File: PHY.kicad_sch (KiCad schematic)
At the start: 19 parts, among them U11 LAN8742A, Y2 25Mhz

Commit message: change cad data
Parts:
- removed C39, C40: 15pF, Capacitor_SMD:C_0603_1608Metric_Pad1.08x0.95mm_HandSolder, symbol Device:C
- removed Y2: 25Mhz, Crystal:Crystal_SMD_SeikoEpson_FA238-4Pin_3.2x2.5mm, symbol Device:Crystal
- added C55, C56, C60: 100n, Capacitor_SMD:C_0603_1608Metric_Pad1.08x0.95mm_HandSolder, symbol Device:C_Small
- added C57, C58: 15pF, Capacitor_SMD:C_0603_1608Metric_Pad1.08x0.95mm_HandSolder, symbol Device:C
- added C62: 1u, Capacitor_SMD:C_0603_1608Metric_Pad1.08x0.95mm_HandSolder, symbol Device:C_Small
- added C63: 470p, Capacitor_SMD:C_0603_1608Metric_Pad1.08x0.95mm_HandSolder, symbol Device:C_Small
- added D10, D11: LED, LED_SMD:LED_0603_1608Metric_Pad1.05x0.95mm_HandSolder, symbol Device:LED
- added R51, R52: 1k, Resistor_SMD:R_0603_1608Metric_Pad0.98x0.95mm_HandSolder, symbol Device:R
- added Y3: 25Mhz, Crystal:Crystal_SMD_SeikoEpson_FA128-4Pin_2.0x1.6mm, symbol Device:Crystal_GND24
- renumbered FB1 to FB3, R24 to R31, R23 to R32, R22 to R33, R25 to R34, R26 to R35, R27 to R36, R28 to R37, R32 to R42, R29 to R43, R36 to R44, R33 to R45, R37 to R46, R39 to R47, R38 to R48, U11 to U12
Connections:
- net +3.3V: now also U12.9 (VDDIO), C56.1
- net GND: now also C55.2, C56.2, C57.2, C58.2, C60.2, C62.2, C63.2, D10.1 (K), D11.1 (K), Y3.2, Y3.4
- net at FB3.2, R35.1, R37.1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: now also C55.1, C60.1
- net at U12.2 (LED2/~{INTSEL}): now also R52.1
- net at U12.3 (LED1/REGOFF): now also R51.1
- net at U12.4 (XTAL2): now also C57.1, Y3.3
- net at U12.5 (XTAL1/CLKIN): now also C58.1, Y3.1
- net at U12.6 (VDDCR): now also C62.1, C63.1
- new net: D10.2 (A), R51.2
- new net: D11.2 (A), R52.2
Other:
- moved on the sheet: R35, R37, R42, R44

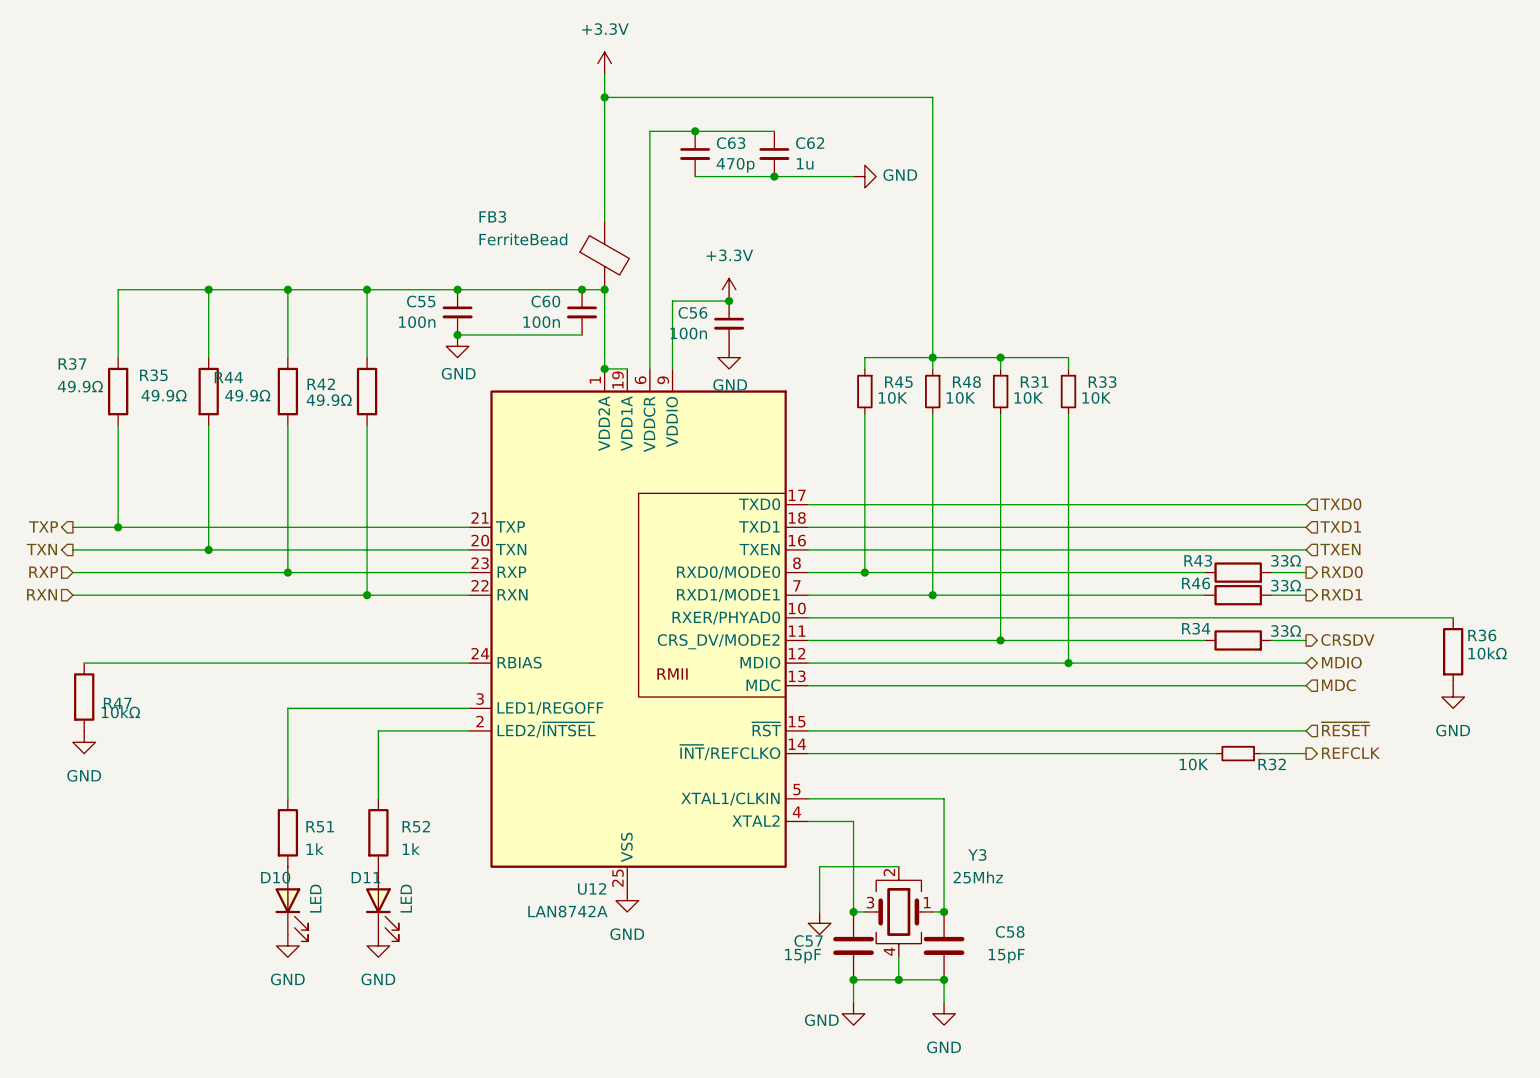
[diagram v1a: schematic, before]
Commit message: remove efuse
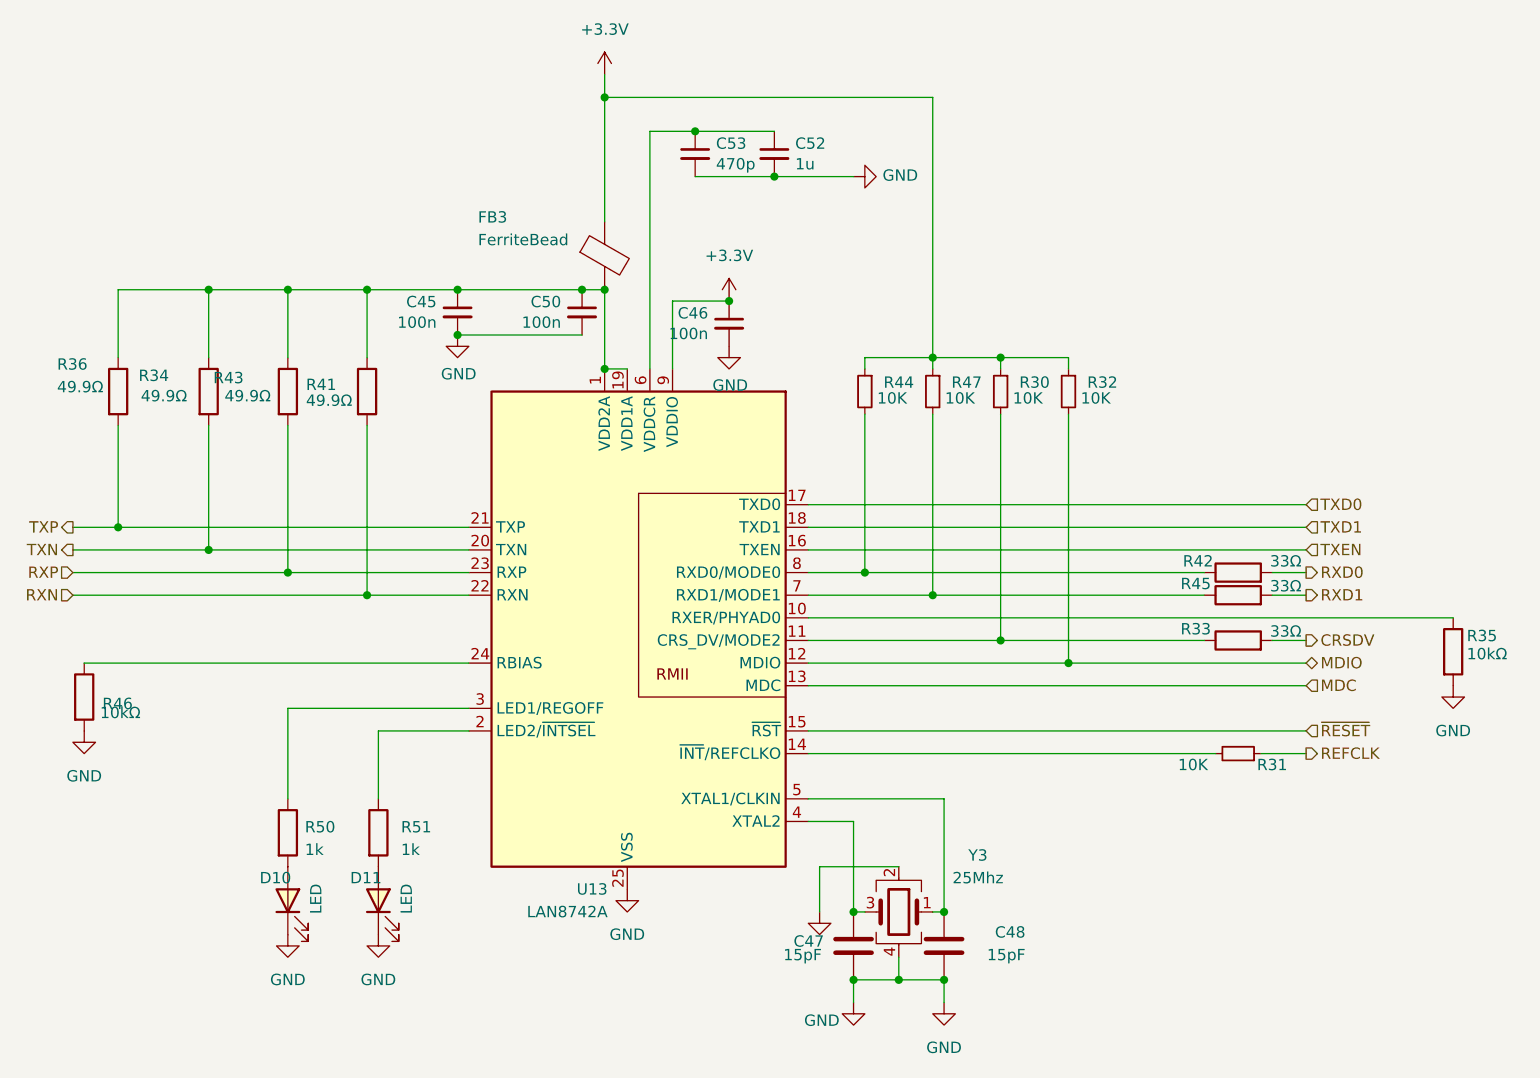
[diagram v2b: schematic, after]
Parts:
- renumbered C55 to C45, C56 to C46, C57 to C47, C58 to C48, C60 to C50, C62 to C52, C63 to C53, R31 to R30, R32 to R31, R33 to R32, R34 to R33, R35 to R34, R36 to R35, R37 to R36, R42 to R41, R43 to R42, R44 to R43, R45 to R44, R46 to R45, R47 to R46, R48 to R47, R51 to R50, R52 to R51, U12 to U13
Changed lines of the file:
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@@
 		(on_board yes)
 		(dnp no)
-		(property "Reference" "R46"
+		(property "Reference" "R45"
 			(at 206.502 115.57 90)
 			(effects
@@
 			(project "mainboard4"
 				(path "/dd07ab80-a59c-44f4-ac7d-849e21e1384e/4fc6aed4-b6ec-46a7-b9d1-1f9060000df7"
-					(reference "R46")
+					(reference "R45")
 					(unit 1)
 				)
@@
 		(on_board yes)
 		(dnp no)
-		(property "Reference" "R44"
+		(property "Reference" "R43"
 			(at 94.488 92.456 0)
 			(effects
@@
 			(project "mainboard4"
 				(path "/dd07ab80-a59c-44f4-ac7d-849e21e1384e/4fc6aed4-b6ec-46a7-b9d1-1f9060000df7"
-					(reference "R44")
+					(reference "R43")
 					(unit 1)
 				)
@@
 		(on_board yes)
 		(dnp no)
-		(property "Reference" "C56"
+		(property "Reference" "C46"
 			(at 150.0632 85.1916 0)
 			(effects
@@
 			(project "mainboard4"
 				(path "/dd07ab80-a59c-44f4-ac7d-849e21e1384e/4fc6aed4-b6ec-46a7-b9d1-1f9060000df7"
-					(reference "C56")
+					(reference "C46")
 					(unit 1)
 				)
@@
 		(on_board yes)
 		(dnp no)
-		(property "Reference" "C60"
+		(property "Reference" "C50"
 			(at 133.5532 83.9216 0)
 			(effects
@@
 			(project "mainboard4"
 				(path "/dd07ab80-a59c-44f4-ac7d-849e21e1384e/4fc6aed4-b6ec-46a7-b9d1-1f9060000df7"
-					(reference "C60")
+					(reference "C50")
 					(unit 1)
 				)
@@
 		(on_board yes)
 		(dnp no)
-		(property "Reference" "R47"
+		(property "Reference" "R46"
 			(at 82.042 129.032 0)
 			(effects
@@
 			(project "mainboard4"
 				(path "/dd07ab80-a59c-44f4-ac7d-849e21e1384e/4fc6aed4-b6ec-46a7-b9d1-1f9060000df7"
-					(reference "R47")
+					(reference "R46")
 					(unit 1)
 				)
@@
 		(on_board yes)
 		(dnp no)
-		(property "Reference" "R37"
+		(property "Reference" "R36"
 			(at 76.962 90.932 0)
 			(effects
@@
 			(project "mainboard4"
 				(path "/dd07ab80-a59c-44f4-ac7d-849e21e1384e/4fc6aed4-b6ec-46a7-b9d1-1f9060000df7"
-					(reference "R37")
+					(reference "R36")
 					(unit 1)
 				)
@@
 		(on_board yes)
 		(dnp no)
-		(property "Reference" "U12"
+		(property "Reference" "U13"
 			(at 138.7759 149.86 0)
 			(effects
@@
 			(project "mainboard4"
 				(path "/dd07ab80-a59c-44f4-ac7d-849e21e1384e/4fc6aed4-b6ec-46a7-b9d1-1f9060000df7"
-					(reference "U12")
+					(reference "U13")
 					(unit 1)
 				)
@@
 		(on_board yes)
 		(dnp no)
-		(property "Reference" "R43"
+		(property "Reference" "R42"
 			(at 206.756 113.03 90)
 			(effects
@@
 			(project "mainboard4"
 				(path "/dd07ab80-a59c-44f4-ac7d-849e21e1384e/4fc6aed4-b6ec-46a7-b9d1-1f9060000df7"
-					(reference "R43")
+					(reference "R42")
 					(unit 1)
 				)
@@
 		(on_board yes)
 		(dnp no)
-		(property "Reference" "R42"
+		(property "Reference" "R41"
 			(at 104.902 93.218 0)
 			(effects
@@
 			(project "mainboard4"
 				(path "/dd07ab80-a59c-44f4-ac7d-849e21e1384e/4fc6aed4-b6ec-46a7-b9d1-1f9060000df7"
-					(reference "R42")
+					(reference "R41")
 					(unit 1)
 				)
@@
 		(on_board yes)
 		(dnp no)
-		(property "Reference" "R36"
+		(property "Reference" "R35"
 			(at 235.204 121.412 0)
 			(effects
@@
 			(project "mainboard4"
 				(path "/dd07ab80-a59c-44f4-ac7d-849e21e1384e/4fc6aed4-b6ec-46a7-b9d1-1f9060000df7"
-					(reference "R36")
+					(reference "R35")
 					(unit 1)
 				)
@@
 		(on_board yes)
 		(dnp no)
-		(property "Reference" "R35"
+		(property "Reference" "R34"
 			(at 86.106 92.202 0)
 			(effects
@@
 			(project "mainboard4"
 				(path "/dd07ab80-a59c-44f4-ac7d-849e21e1384e/4fc6aed4-b6ec-46a7-b9d1-1f9060000df7"
-					(reference "R35")
+					(reference "R34")
 					(unit 1)
 				)
@@
 		(on_board yes)
 		(dnp no)
-		(property "Reference" "C62"
+		(property "Reference" "C52"
 			(at 159.8168 66.1416 0)
 			(effects
@@
 			(project "mainboard4"
 				(path "/dd07ab80-a59c-44f4-ac7d-849e21e1384e/4fc6aed4-b6ec-46a7-b9d1-1f9060000df7"
-					(reference "C62")
+					(reference "C52")
 					(unit 1)
 				)
@@
 		(on_board yes)
 		(dnp no)
-		(property "Reference" "R48"
+		(property "Reference" "R47"
 			(at 179.07 92.964 0)
 			(effects
@@
 			(project "mainboard4"
 				(path "/dd07ab80-a59c-44f4-ac7d-849e21e1384e/4fc6aed4-b6ec-46a7-b9d1-1f9060000df7"
-					(reference "R48")
+					(reference "R47")
 					(unit 1)
 				)
@@
 		(on_board yes)
 		(dnp no)
-		(property "Reference" "C63"
+		(property "Reference" "C53"
 			(at 150.9268 66.1416 0)
 			(effects
@@
 			(project "mainboard4"
 				(path "/dd07ab80-a59c-44f4-ac7d-849e21e1384e/4fc6aed4-b6ec-46a7-b9d1-1f9060000df7"
-					(reference "C63")
+					(reference "C53")
 					(unit 1)
 				)
@@
 		(dnp no)
 		(fields_autoplaced yes)
-		(property "Reference" "R51"
+		(property "Reference" "R50"
 			(at 104.775 142.875 0)
 			(effects
@@
 			(project "mainboard4"
 				(path "/dd07ab80-a59c-44f4-ac7d-849e21e1384e/4fc6aed4-b6ec-46a7-b9d1-1f9060000df7"
-					(reference "R51")
+					(reference "R50")
 					(unit 1)
 				)
@@
 		(on_board yes)
 		(dnp no)
-		(property "Reference" "R45"
+		(property "Reference" "R44"
 			(at 171.45 92.964 0)
 			(effects
@@
 			(project "mainboard4"
 				(path "/dd07ab80-a59c-44f4-ac7d-849e21e1384e/4fc6aed4-b6ec-46a7-b9d1-1f9060000df7"
-					(reference "R45")
+					(reference "R44")
 					(unit 1)
 				)
@@
 		(on_board yes)
 		(dnp no)
-		(property "Reference" "R33"
+		(property "Reference" "R32"
 			(at 194.31 92.964 0)
 			(effects
@@
 			(project "mainboard4"
 				(path "/dd07ab80-a59c-44f4-ac7d-849e21e1384e/4fc6aed4-b6ec-46a7-b9d1-1f9060000df7"
-					(reference "R33")
+					(reference "R32")
 					(unit 1)
 				)
@@
 		(dnp no)
 		(fields_autoplaced yes)
-		(property "Reference" "R52"
+		(property "Reference" "R51"
 			(at 115.57 142.875 0)
 			(effects
@@
 			(project "mainboard4"
 				(path "/dd07ab80-a59c-44f4-ac7d-849e21e1384e/4fc6aed4-b6ec-46a7-b9d1-1f9060000df7"
-					(reference "R52")
+					(reference "R51")
 					(unit 1)
 				)
@@
 		(on_board yes)
 		(dnp no)
-		(property "Reference" "R32"
+		(property "Reference" "R31"
 			(at 213.36 135.89 90)
 			(effects
@@
 			(project "mainboard4"
 				(path "/dd07ab80-a59c-44f4-ac7d-849e21e1384e/4fc6aed4-b6ec-46a7-b9d1-1f9060000df7"
-					(reference "R32")
+					(reference "R31")
 					(unit 1)
 				)
@@
 		(on_board yes)
 		(dnp no)
-		(property "Reference" "C58"
+		(property "Reference" "C48"
 			(at 185.674 154.686 0)
 			(effects
@@
 			(project "mainboard4"
 				(path "/dd07ab80-a59c-44f4-ac7d-849e21e1384e/4fc6aed4-b6ec-46a7-b9d1-1f9060000df7"
-					(reference "C58")
+					(reference "C48")
 					(unit 1)
 				)
@@
 		(on_board yes)
 		(dnp no)
-		(property "Reference" "R31"
+		(property "Reference" "R30"
 			(at 186.69 92.964 0)
 			(effects
@@
 			(project "mainboard4"
 				(path "/dd07ab80-a59c-44f4-ac7d-849e21e1384e/4fc6aed4-b6ec-46a7-b9d1-1f9060000df7"
-					(reference "R31")
+					(reference "R30")
 					(unit 1)
 				)
@@
 		(on_board yes)
 		(dnp no)
-		(property "Reference" "C55"
+		(property "Reference" "C45"
 			(at 119.5832 83.9216 0)
 			(effects
@@
 			(project "mainboard4"
 				(path "/dd07ab80-a59c-44f4-ac7d-849e21e1384e/4fc6aed4-b6ec-46a7-b9d1-1f9060000df7"
-					(reference "C55")
+					(reference "C45")
 					(unit 1)
 				)
@@
 		(on_board yes)
 		(dnp no)
-		(property "Reference" "C57"
+		(property "Reference" "C47"
 			(at 163.068 155.702 0)
 			(effects
@@
 			(project "mainboard4"
 				(path "/dd07ab80-a59c-44f4-ac7d-849e21e1384e/4fc6aed4-b6ec-46a7-b9d1-1f9060000df7"
-					(reference "C57")
+					(reference "C47")
 					(unit 1)
 				)
@@
 		(on_board yes)
 		(dnp no)
-		(property "Reference" "R34"
+		(property "Reference" "R33"
 			(at 206.502 120.65 90)
 			(effects
@@
 			(project "mainboard4"
 				(path "/dd07ab80-a59c-44f4-ac7d-849e21e1384e/4fc6aed4-b6ec-46a7-b9d1-1f9060000df7"
-					(reference "R34")
+					(reference "R33")
 					(unit 1)
 				)
